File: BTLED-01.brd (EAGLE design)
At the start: 85.1 x 58.4 mm, 17 parts

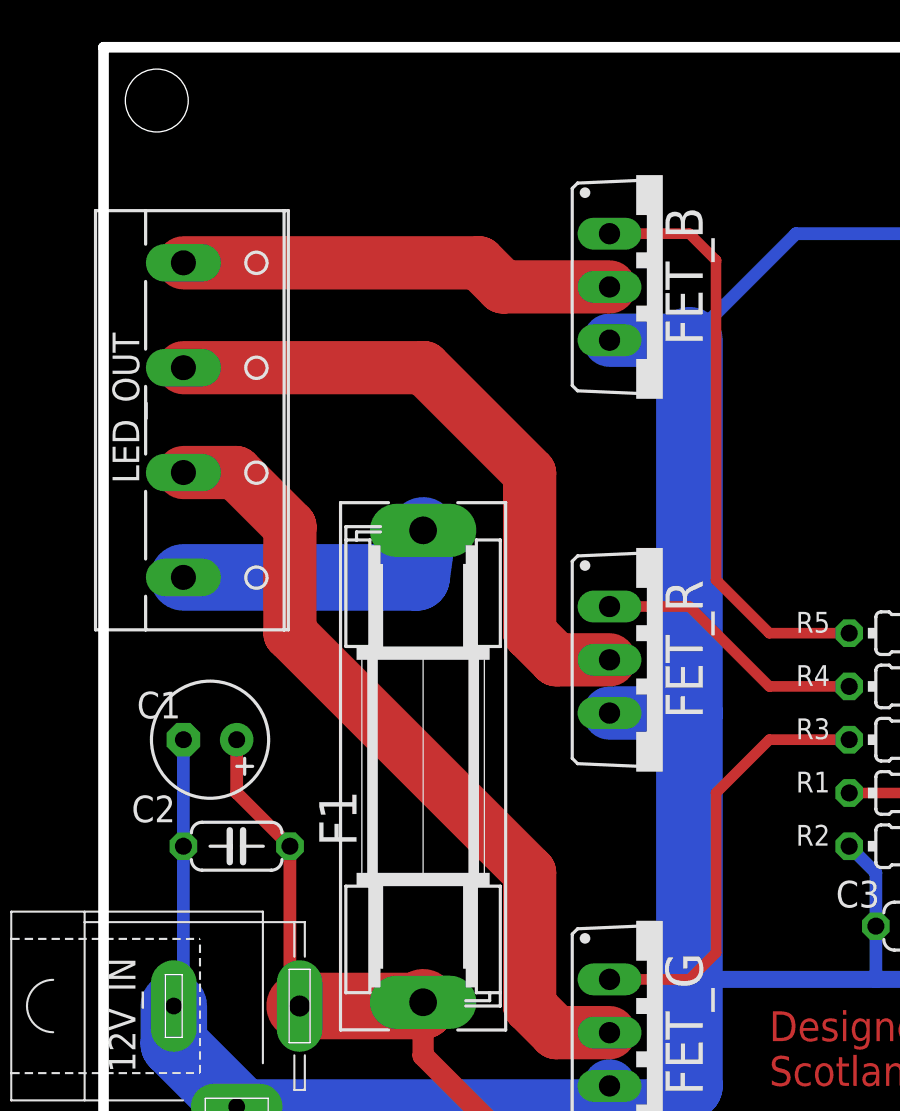
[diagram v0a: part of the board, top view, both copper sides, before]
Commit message: feat: Add BRG+ labels to upper copper mask
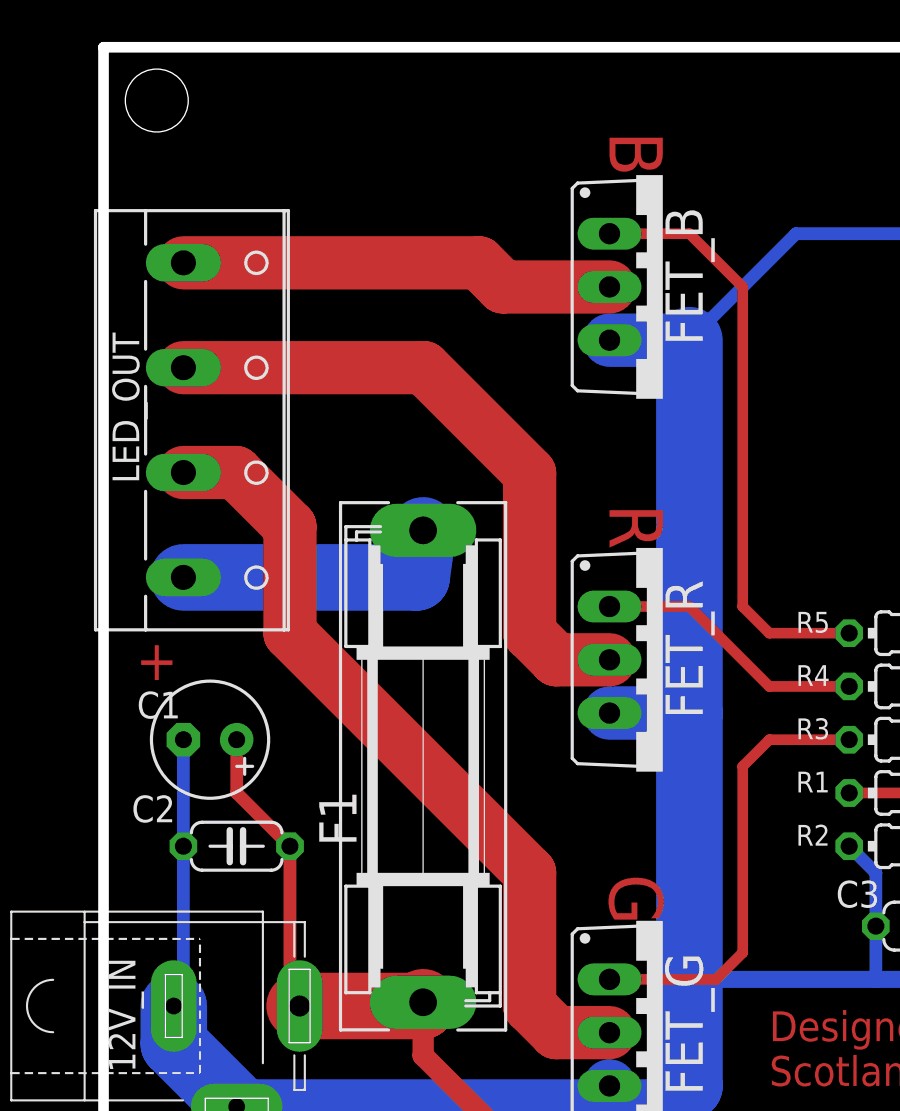
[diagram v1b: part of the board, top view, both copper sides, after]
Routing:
- net G_SIG_2: track 20.6 -> 21.4 mm
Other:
- board text added: "+"
- board text added: "B"
- board text added: "G"
- board text added: "R"
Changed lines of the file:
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@@
 <text x="60.96" y="35.56" size="5.08" layer="1" font="vector" ratio="12" grouprefs="INFO_TEXT">F#</text>
 <text x="69.85" y="35.56" size="1.6764" layer="1" font="vector" ratio="10" grouprefs="INFO_TEXT">07/20</text>
+<text x="0" y="57.15" size="1.9304" layer="1" font="vector" align="center">+</text>
+<text x="22.86" y="63.5" size="2.54" layer="1" font="vector" ratio="10" rot="SR270" align="center">R</text>
+<text x="22.86" y="45.72" size="2.54" layer="1" font="vector" ratio="10" rot="SR270" align="center">G</text>
+<text x="22.86" y="81.28" size="2.54" layer="1" font="vector" ratio="10" rot="SR270" align="center">B</text>
 </plain>
 <attributes>
@@
 <contactref element="FET_G" pad="G"/>
 <contactref element="R3" pad="1"/>
-<wire x1="21.59" y1="41.91" x2="25.4" y2="41.91" width="0.508" layer="1"/>
-<wire x1="25.4" y1="41.91" x2="26.67" y2="43.18" width="0.508" layer="1"/>
-<wire x1="26.67" y1="50.8" x2="29.21" y2="53.34" width="0.508" layer="1"/>
+<wire x1="21.59" y1="41.91" x2="26.67" y2="41.91" width="0.508" layer="1"/>
+<wire x1="26.67" y1="41.91" x2="27.94" y2="43.18" width="0.508" layer="1"/>
+<wire x1="27.94" y1="52.07" x2="29.21" y2="53.34" width="0.508" layer="1"/>
 <wire x1="29.21" y1="53.34" x2="33.02" y2="53.34" width="0.508" layer="1"/>
-<wire x1="26.67" y1="43.18" x2="26.67" y2="50.8" width="0.508" layer="1"/>
+<wire x1="27.94" y1="43.18" x2="27.94" y2="52.07" width="0.508" layer="1"/>
 </signal>
 <signal name="R_SIG_2">
@@
 <contactref element="R5" pad="1"/>
 <wire x1="21.59" y1="77.47" x2="25.4" y2="77.47" width="0.508" layer="1"/>
-<wire x1="25.4" y1="77.47" x2="26.67" y2="76.2" width="0.508" layer="1"/>
+<wire x1="25.4" y1="77.47" x2="27.94" y2="74.93" width="0.508" layer="1"/>
 <wire x1="29.21" y1="58.42" x2="33.02" y2="58.42" width="0.508" layer="1"/>
-<wire x1="26.67" y1="76.2" x2="26.67" y2="60.96" width="0.508" layer="1"/>
-<wire x1="26.67" y1="60.96" x2="29.21" y2="58.42" width="0.508" layer="1"/>
+<wire x1="27.94" y1="74.93" x2="27.94" y2="59.69" width="0.508" layer="1"/>
+<wire x1="27.94" y1="59.69" x2="29.21" y2="58.42" width="0.508" layer="1"/>
 </signal>
 <signal name="N$1" class="1">

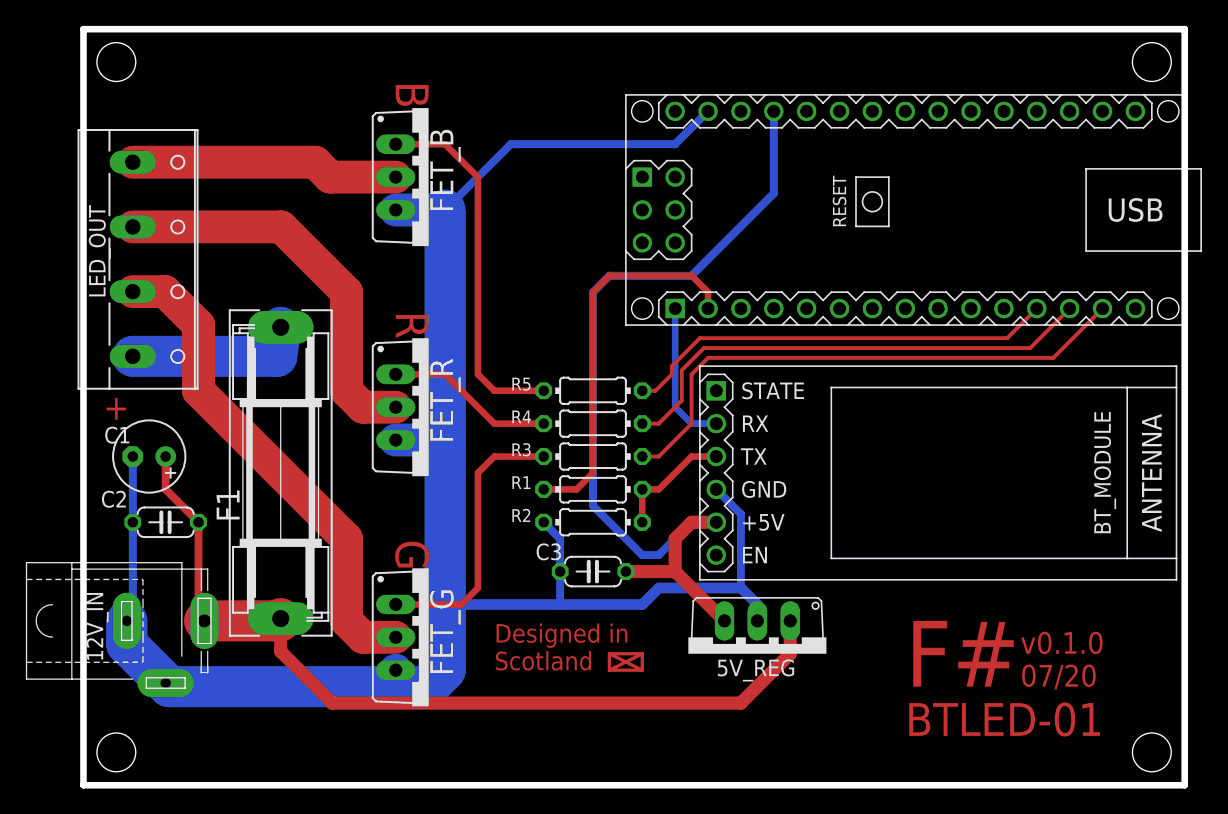
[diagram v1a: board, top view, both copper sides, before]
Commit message: fix: tweak fastener holes for easier printing
also moved some traces a tad
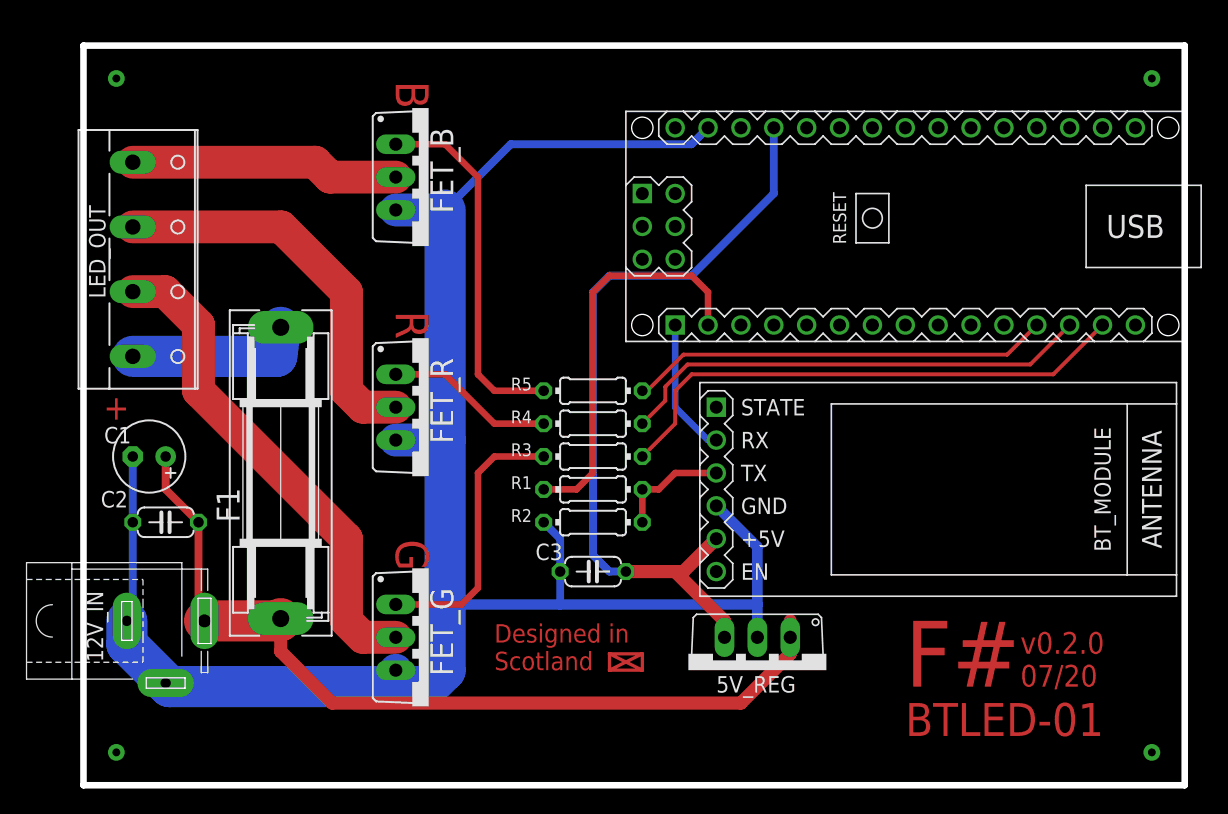
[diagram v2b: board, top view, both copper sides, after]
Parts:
- moved 5V_REG 1.27 mm to (49.5, 36.8)
- moved BT_MODULE 1.27 mm to (63.5, 50.8)
- moved ARDUINO_NANO 1.27 mm to (61.0, 71.1)
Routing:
- net 5V: track 67.6 -> 60.3 mm
- net R_SIG_1: track 38.1 -> 36.8 mm
- net G_SIG_1: track 42.5 -> 41.3 mm
- net BT_TX_5V: track 29.5 -> 30.8 mm
- net B_SIG_1: track 33.5 -> 32.6 mm
- net BT_RX: track 11.3 -> 10.6 mm
- net BT_TX_3.3V: track 9.31 -> 8.78 mm
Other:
- board size 85.1 x 58.4 mm -> 85.1 x 57.2 mm
- board text added: "v0.2.0"
- board text removed: "v0.1.0"
